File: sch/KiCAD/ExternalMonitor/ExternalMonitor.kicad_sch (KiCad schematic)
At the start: 29 parts, among them J1 Conn_01x02_Male, J10 Conn_01x04_Female, J11 Conn_01x08_Female, J12 Conn_01x04_Female, J13 Conn_01x15, J14 Conn_01x03_Pin, J2 Conn_01x02_Male, J3 Conn_01x03_Male, J4 Conn_01x03_Male, J5 Conn_01x03_Female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

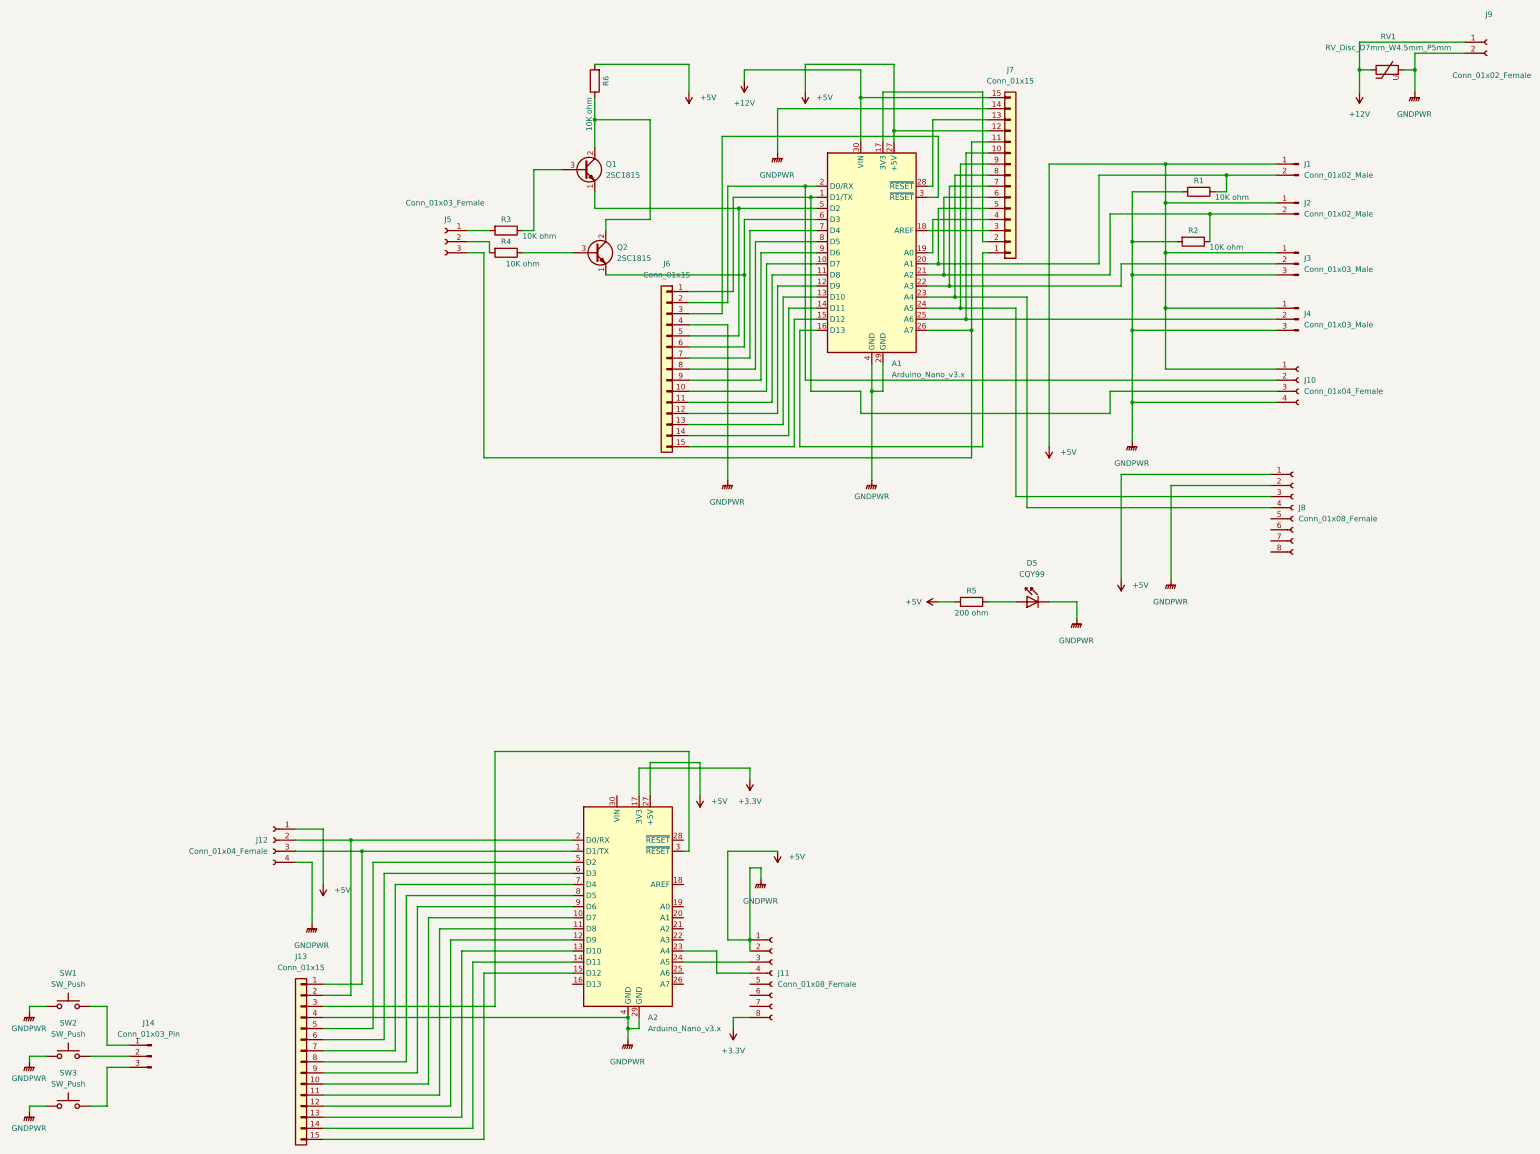
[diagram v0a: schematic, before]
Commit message: 複製した回路図の重複部分を削除
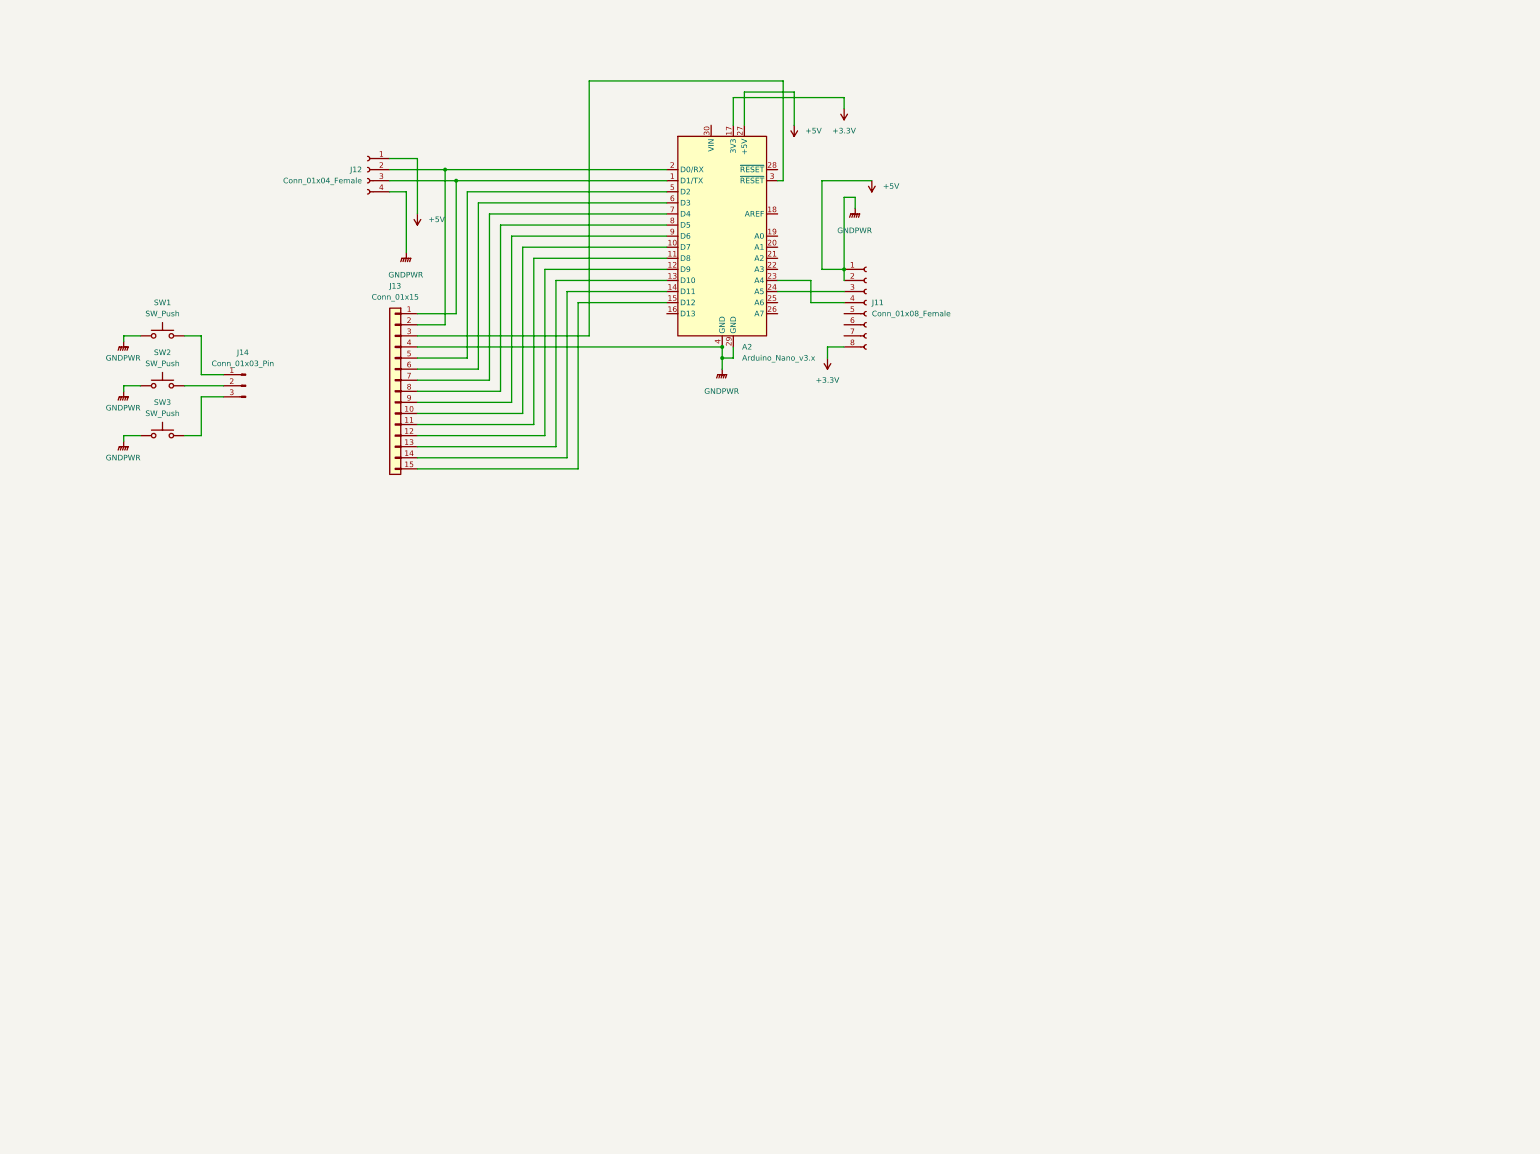
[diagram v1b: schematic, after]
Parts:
- removed A1: Arduino_Nano_v3.x, Module:Arduino_Nano, symbol MCU_Module:Arduino_Nano_v3.x
- removed D5: CQY99, LED_THT:LED_D5.0mm_IRGrey, symbol LED:CQY99
- removed J1, J2: Conn_01x02_Male, Connector_Molex:Molex_SPOX_5268-02A_1x02_P2.50mm_Horizontal, symbol Connector:Conn_01x02_Male
- removed J10: Conn_01x04_Female, Connector_Molex:Molex_SPOX_5268-04A_1x04_P2.50mm_Horizontal, symbol Connector:Conn_01x04_Female
- removed J3, J4: Conn_01x03_Male, Connector_Molex:Molex_SPOX_5268-03A_1x03_P2.50mm_Horizontal, symbol Connector:Conn_01x03_Male
- removed J5: Conn_01x03_Female, Connector_Molex:Molex_KK-254_AE-6410-03A_1x03_P2.54mm_Vertical, symbol Connector:Conn_01x03_Female
- removed J6, J7: Conn_01x15, Connector_PinSocket_2.54mm:PinSocket_1x15_P2.54mm_Vertical, symbol Connector_Generic:Conn_01x15
- removed J8: Conn_01x08_Female, Connector_JST:JST_XH_S8B-XH-A-1_1x08_P2.50mm_Horizontal, symbol Connector:Conn_01x08_Female
- removed J9: Conn_01x02_Female, Connector_Molex:Molex_KK-254_AE-6410-02A_1x02_P2.54mm_Vertical, symbol Connector:Conn_01x02_Female
- removed Q1, Q2: 2SC1815, Package_TO_SOT_THT:TO-92_Inline, symbol Transistor_BJT:2SC1815
- removed R1, R2, R3, R4, R6: 10K ohm, Resistor_THT:R_Axial_DIN0204_L3.6mm_D1.6mm_P7.62mm_Horizontal, symbol Device:R
- removed R5: 200 ohm, Resistor_THT:R_Axial_DIN0204_L3.6mm_D1.6mm_P7.62mm_Horizontal, symbol Device:R
- removed RV1: RV_Disc_D7mm_W4.5mm_P5mm, Varistor:RV_Disc_D7mm_W4.5mm_P5mm, symbol Device:Varistor
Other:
- moved on the sheet: A2, J11, J12, J13, J14, SW1, SW2, SW3
